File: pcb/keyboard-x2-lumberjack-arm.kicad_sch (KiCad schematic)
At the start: 141 parts, among them J1 16-pin USB-C Connector SMD, U1 STM32F103 Bluepill, or MiniF4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, U2 SN74LVC1T45DBV

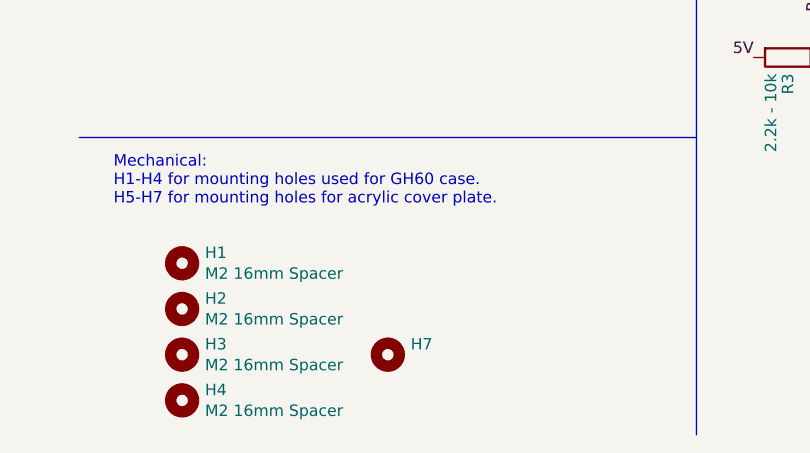
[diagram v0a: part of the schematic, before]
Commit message: fix: update gh60 mounting hole footprint
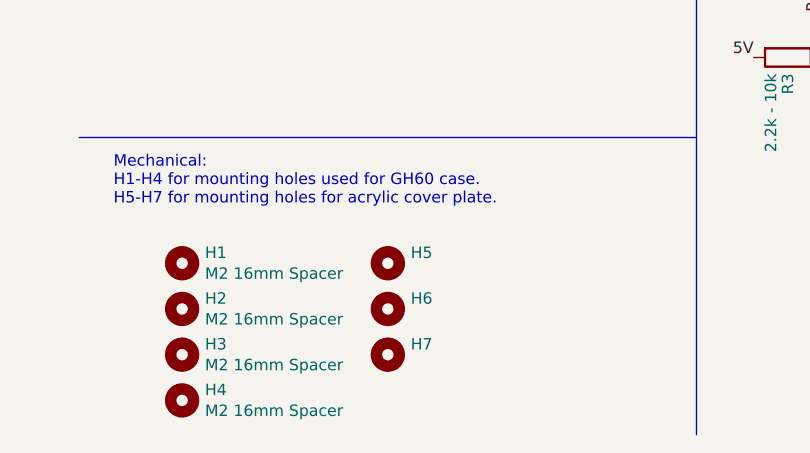
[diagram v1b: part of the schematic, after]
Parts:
- added H5, H6: ~, Lumberjack:MountingSlot_M2, symbol Mechanical:MountingHole
- H7: footprint ProjectLocal:H_M2_Spacer_Hole -> Lumberjack:MountingSlot_M2
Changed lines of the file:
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@@
       (effects (font (size 1.27 1.27)) (justify left))
     )
-    (property "Footprint" "ProjectLocal:H_M2_Spacer_Hole" (id 2) (at 46.99 189.23 0)
+    (property "Footprint" "Lumberjack:MountingSlot_M2" (id 2) (at 46.99 189.23 0)
       (effects (font (size 1.27 1.27)) hide)
     )
@@
     (pin "2")
   )
+  (symbol (lib_id "Mechanical:MountingHole") (at 46.99 184.15 0) (unit 1)
+    (in_bom yes) (on_board yes)
+    (property "Reference" "H6" (id 0) (at 49.53 182.9816 0)
+      (effects (font (size 1.27 1.27)) (justify left))
+    )
+    (property "Value" "~" (id 1) (at 49.53 185.293 0)
+      (effects (font (size 1.27 1.27)) (justify left))
+    )
+    (property "Footprint" "Lumberjack:MountingSlot_M2" (id 2) (at 46.99 184.15 0)
+      (effects (font (size 1.27 1.27)) hide)
+    )
+    (property "Datasheet" "~" (id 3) (at 46.99 184.15 0)
+      (effects (font (size 1.27 1.27)) hide)
+    )
+    (property "Description" "GH-60 Case Mounting Hole" (id 4) (at 46.99 184.15 0)
+      (effects (font (size 1.27 1.27)) hide)
+    )
+  )
+  (symbol (lib_id "Mechanical:MountingHole") (at 46.99 179.07 0) (unit 1)
+    (in_bom yes) (on_board yes)
+    (property "Reference" "H5" (id 0) (at 49.53 177.9016 0)
+      (effects (font (size 1.27 1.27)) (justify left))
+    )
+    (property "Value" "~" (id 1) (at 49.53 180.213 0)
+      (effects (font (size 1.27 1.27)) (justify left))
+    )
+    (property "Footprint" "Lumberjack:MountingSlot_M2" (id 2) (at 46.99 179.07 0)
+      (effects (font (size 1.27 1.27)) hide)
+    )
+    (property "Datasheet" "~" (id 3) (at 46.99 179.07 0)
+      (effects (font (size 1.27 1.27)) hide)
+    )
+    (property "Description" "GH-60 Case Mounting Hole" (id 4) (at 46.99 179.07 0)
+      (effects (font (size 1.27 1.27)) hide)
+    )
+  )
   (sheet_instances
     (path "/" (page "1"))
@@
       (reference "H4") (unit 1) (value "M2 16mm Spacer") (footprint "MountingHole:MountingHole_2.2mm_M2_DIN965_Pad")
     )
+    (path "/9daae529-3d87-482a-896e-85736deff02b"
+      (reference "H5") (unit 1) (value "~") (footprint "Lumberjack:MountingSlot_M2")
+    )
+    (path "/6775a7e8-768f-4d8d-8747-f5103880f760"
+      (reference "H6") (unit 1) (value "~") (footprint "Lumberjack:MountingSlot_M2")
+    )
     (path "/00000000-0000-0000-0000-0000603c4d5a"
-      (reference "H7") (unit 1) (value "~") (footprint "ProjectLocal:H_M2_Spacer_Hole")
+      (reference "H7") (unit 1) (value "~") (footprint "Lumberjack:MountingSlot_M2")
     )
     (path "/00000000-0000-0000-0000-000061bfb907"

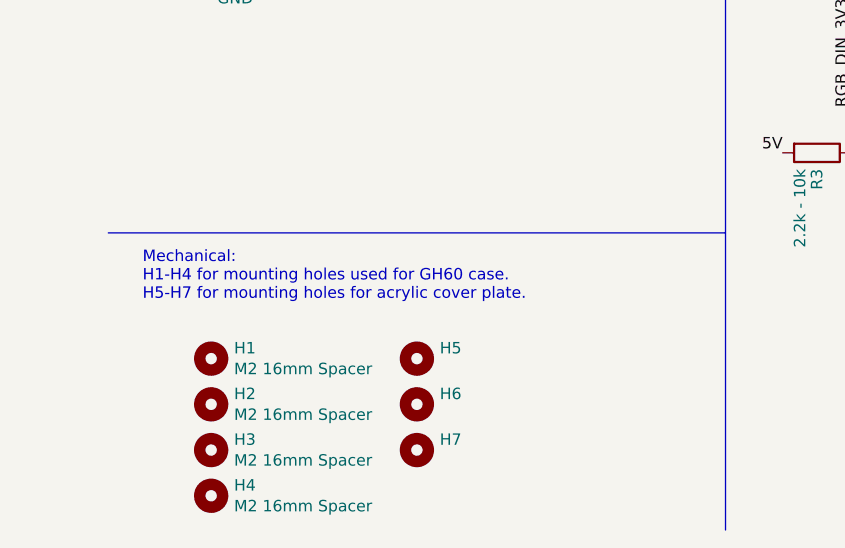
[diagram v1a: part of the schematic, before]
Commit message: fix: update schematic hole mounting hole description
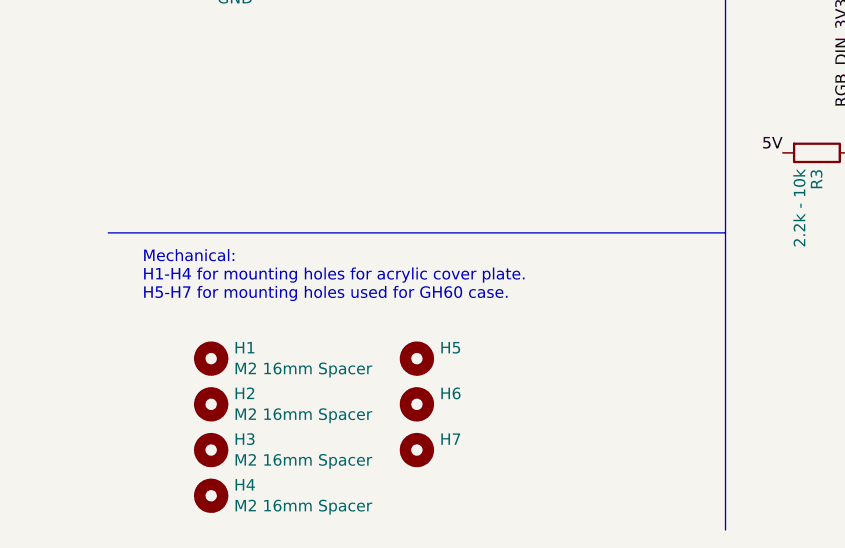
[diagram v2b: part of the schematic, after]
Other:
- note added: "Mechanical: H1-H4 for mounting holes for acrylic cover plate. H5-H7 for mounting holes used for GH60 case."
- note removed: "Mechanical: H1-H4 for mounting holes used for GH60 case. H5-H7 for mounting holes for acrylic cover plate."
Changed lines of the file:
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@@
     (effects (font (size 1.27 1.27)) (justify left bottom))
   )
-  (text "Mechanical:\nH1-H4 for mounting holes used for GH60 case.\nH5-H7 for mounting holes for acrylic cover plate."
+  (text "Mechanical:\nH1-H4 for mounting holes for acrylic cover plate.\nH5-H7 for mounting holes used for GH60 case."
     (at 16.51 172.72 0)
     (effects (font (size 1.27 1.27)) (justify left bottom))
